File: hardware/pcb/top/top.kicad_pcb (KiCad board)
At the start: 2 copper layers, 65 x 120 mm, 33 parts, among them J1 OLED_128x32, J2 Conn_01x15, SW1 SLW-864574-5A-RA-N-D, SW2 RotaryEncoder_Switch

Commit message: finalized plate design
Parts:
- moved J1 1.77 mm to (121.2, 45.0)
- moved SW1 1.28 mm to (122.9, 36.7)
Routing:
- net OLED_SDA: track 119.9 -> 123.6 mm
- net +3.3V: track 136.4 -> 138.9 mm
- net OLED_SCL: track 119.7 -> 121.7 mm
- net BT_SELECT: track 198.0 -> 198.5 mm

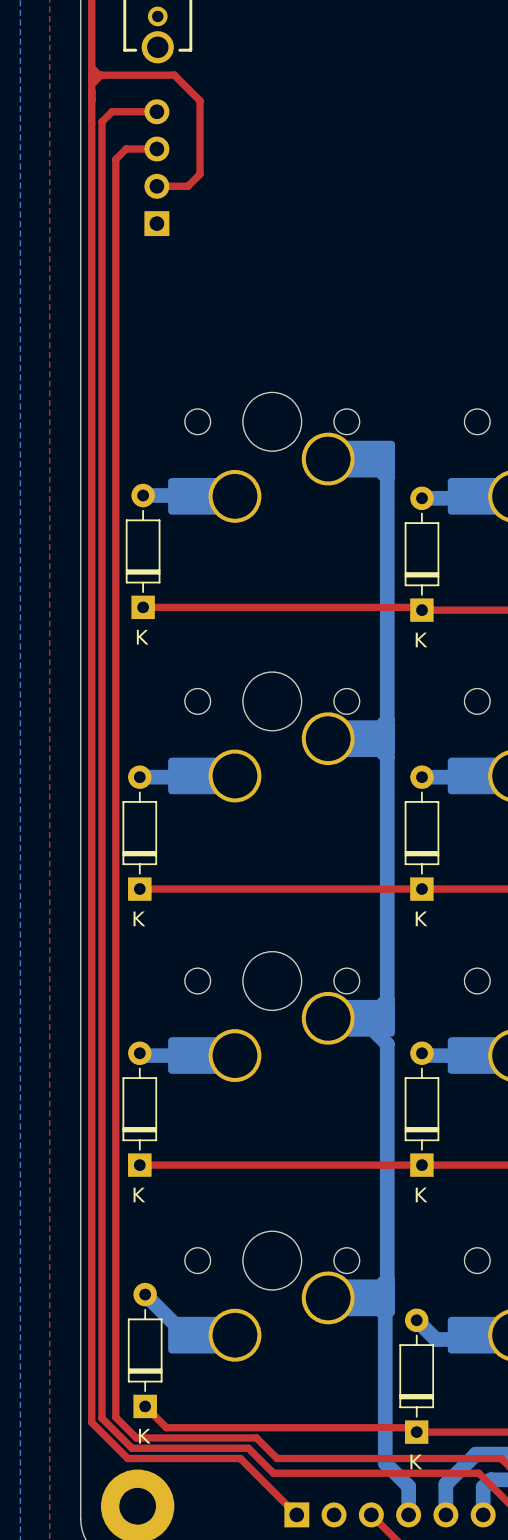
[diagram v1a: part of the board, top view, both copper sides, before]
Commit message: migrate kicad projects from v8 to v9
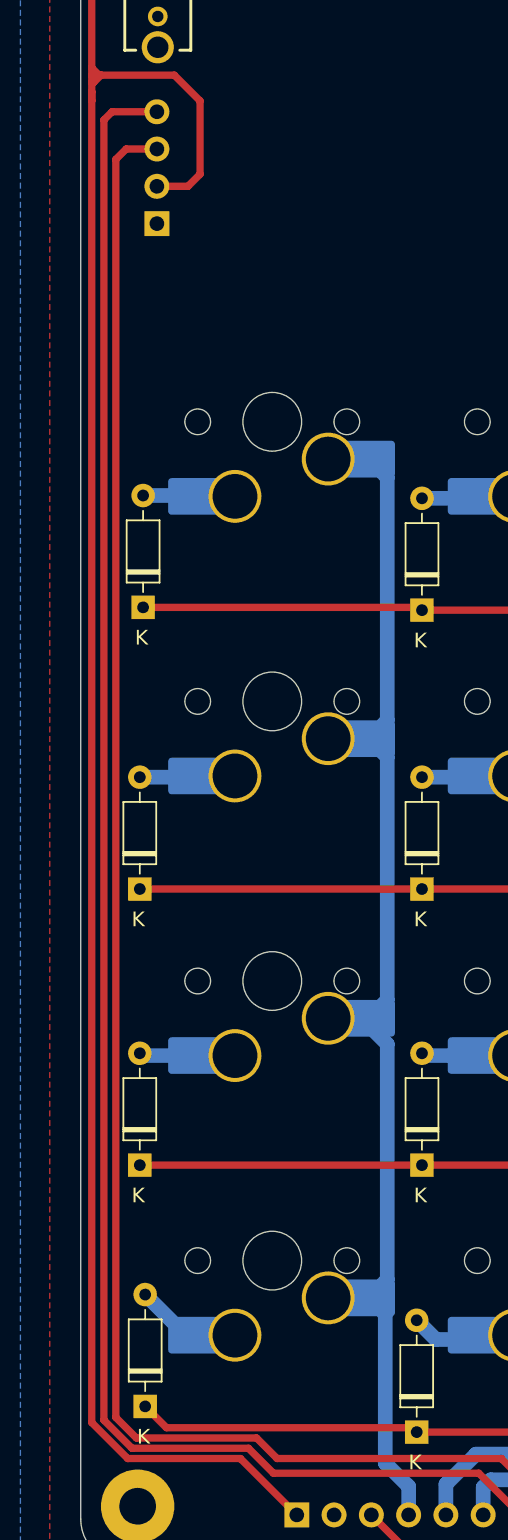
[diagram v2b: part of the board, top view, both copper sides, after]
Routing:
- net Net-(D10-A): track 4.49 -> 3.91 mm

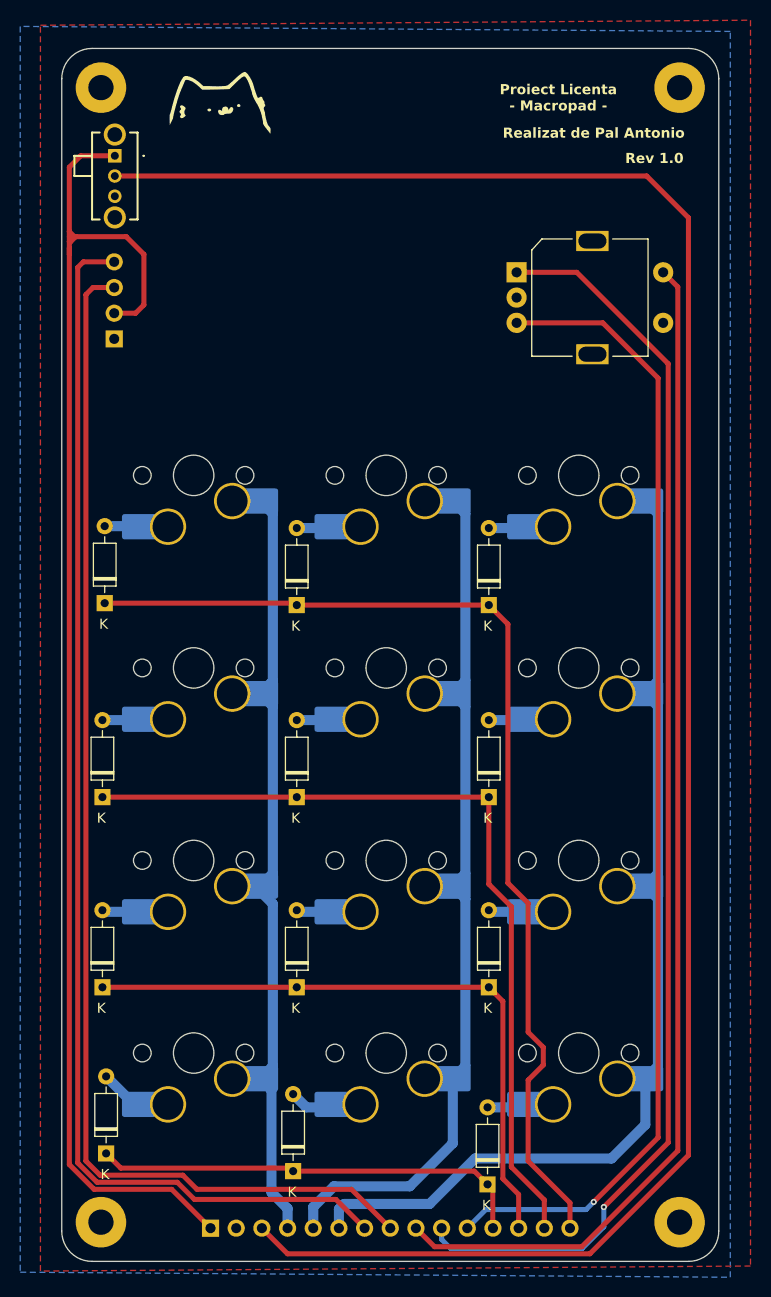
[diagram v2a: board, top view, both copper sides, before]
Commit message: Optimize routing and improve grounding
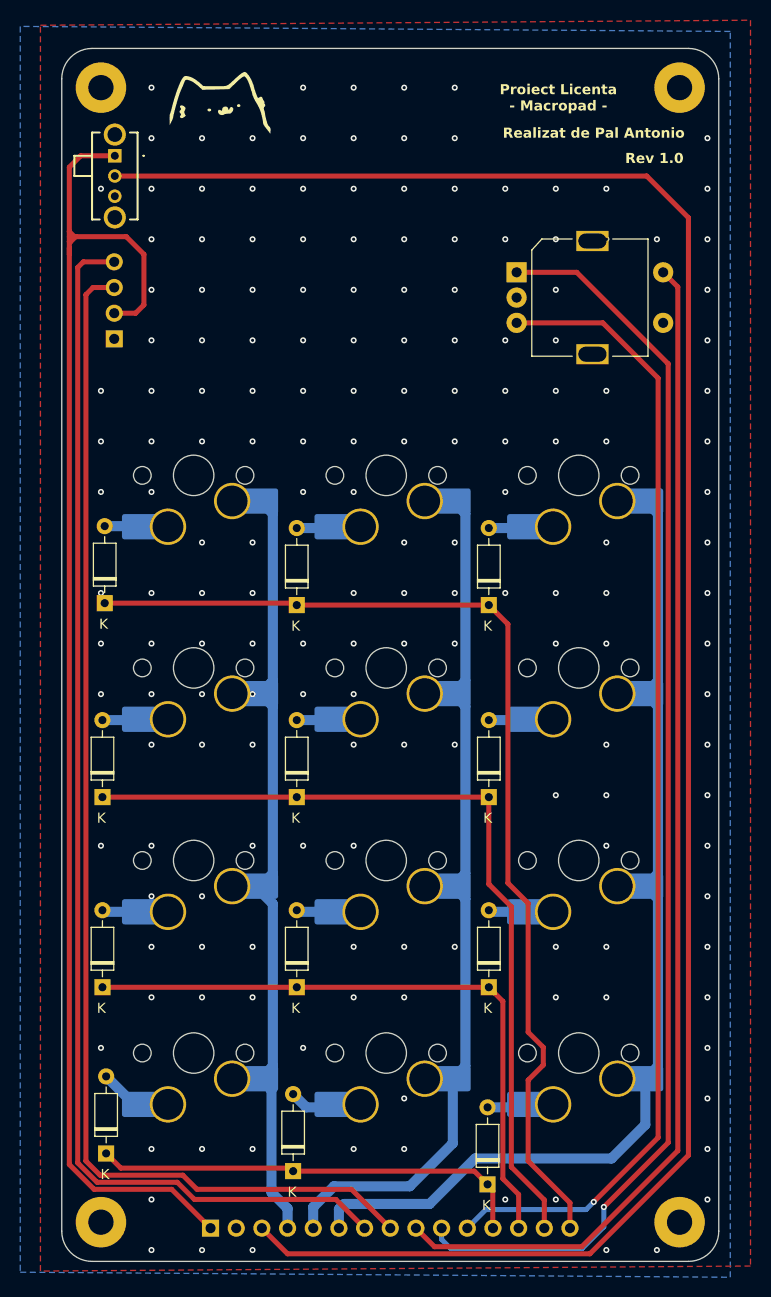
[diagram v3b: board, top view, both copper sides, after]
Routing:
- net GND: vias 0 -> 179

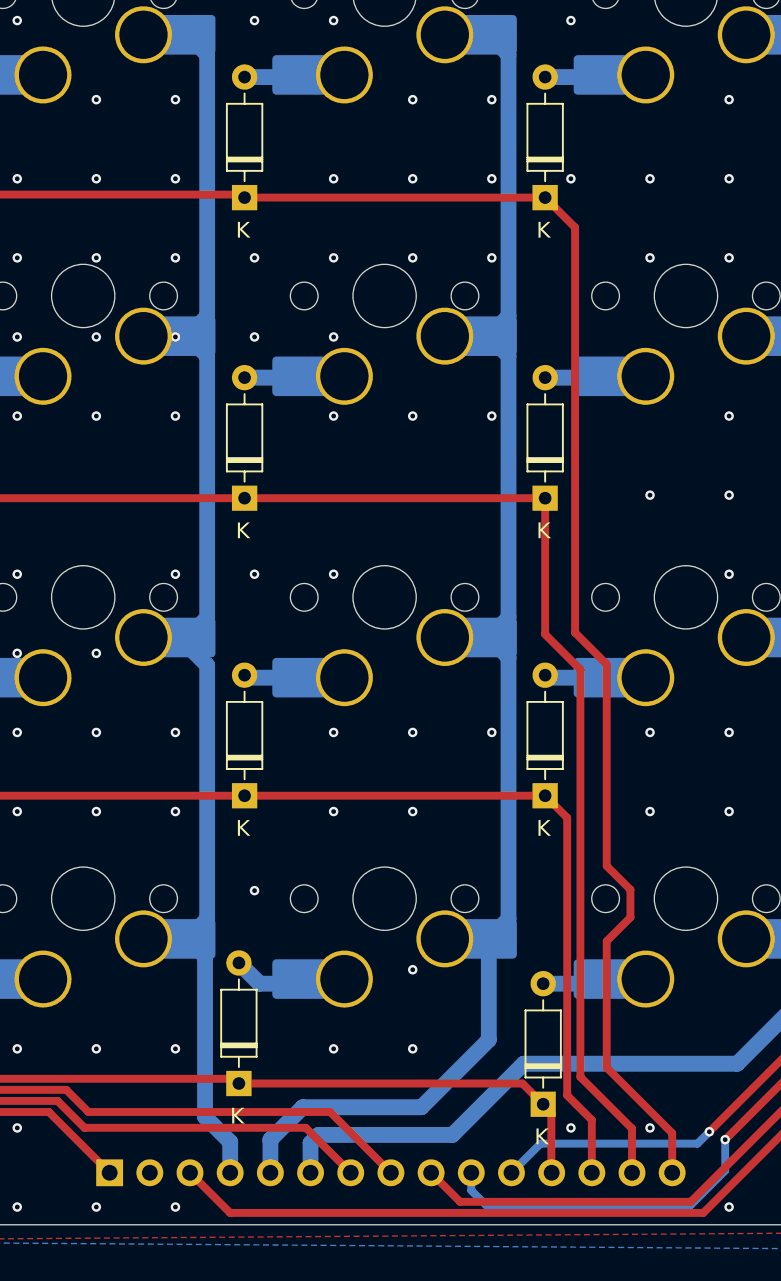
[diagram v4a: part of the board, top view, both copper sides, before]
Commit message: update documentation images, remove copper pours and vias from top plate, minor fixes
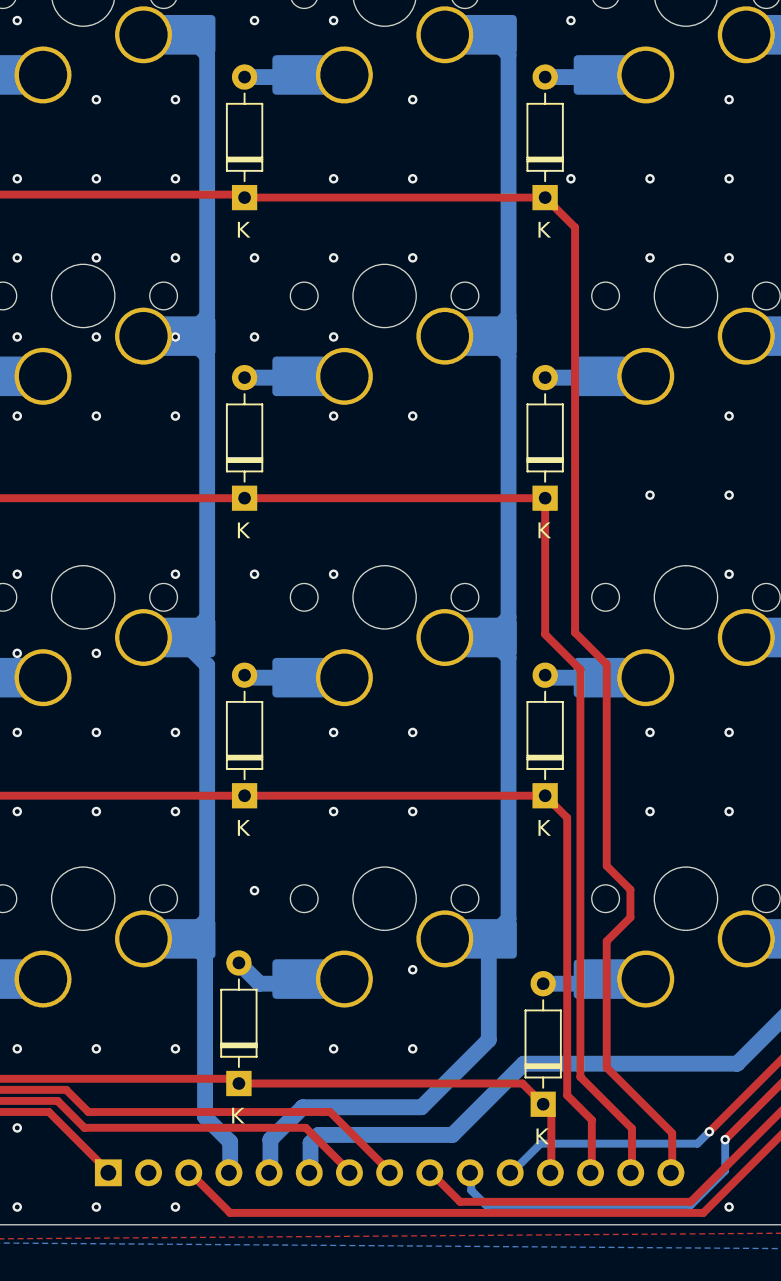
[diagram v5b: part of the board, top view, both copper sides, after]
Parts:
- moved J2 0.08 mm to (132.3, 142.8)
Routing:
- net GND: vias 179 -> 172

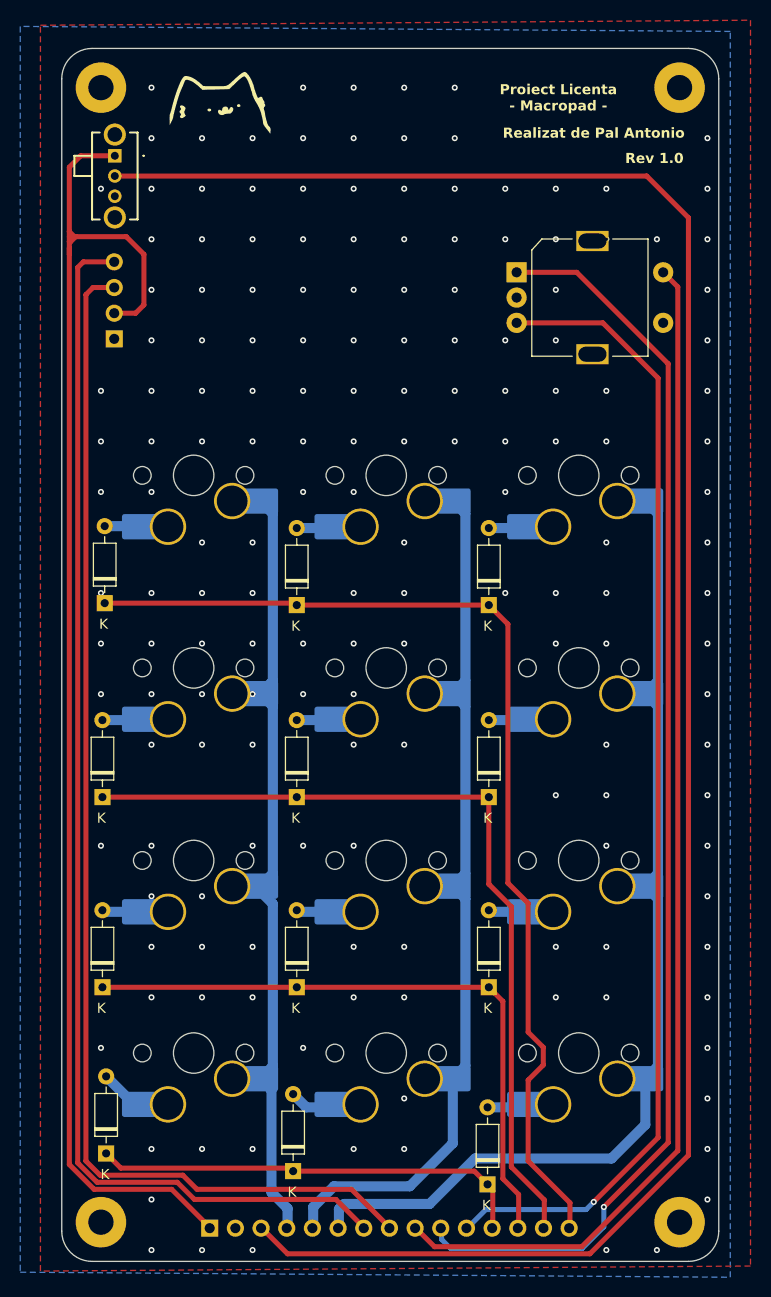
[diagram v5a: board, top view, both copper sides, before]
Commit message: changed m2.5 mh to m2, added screws and nuts to enclosure.FCStd
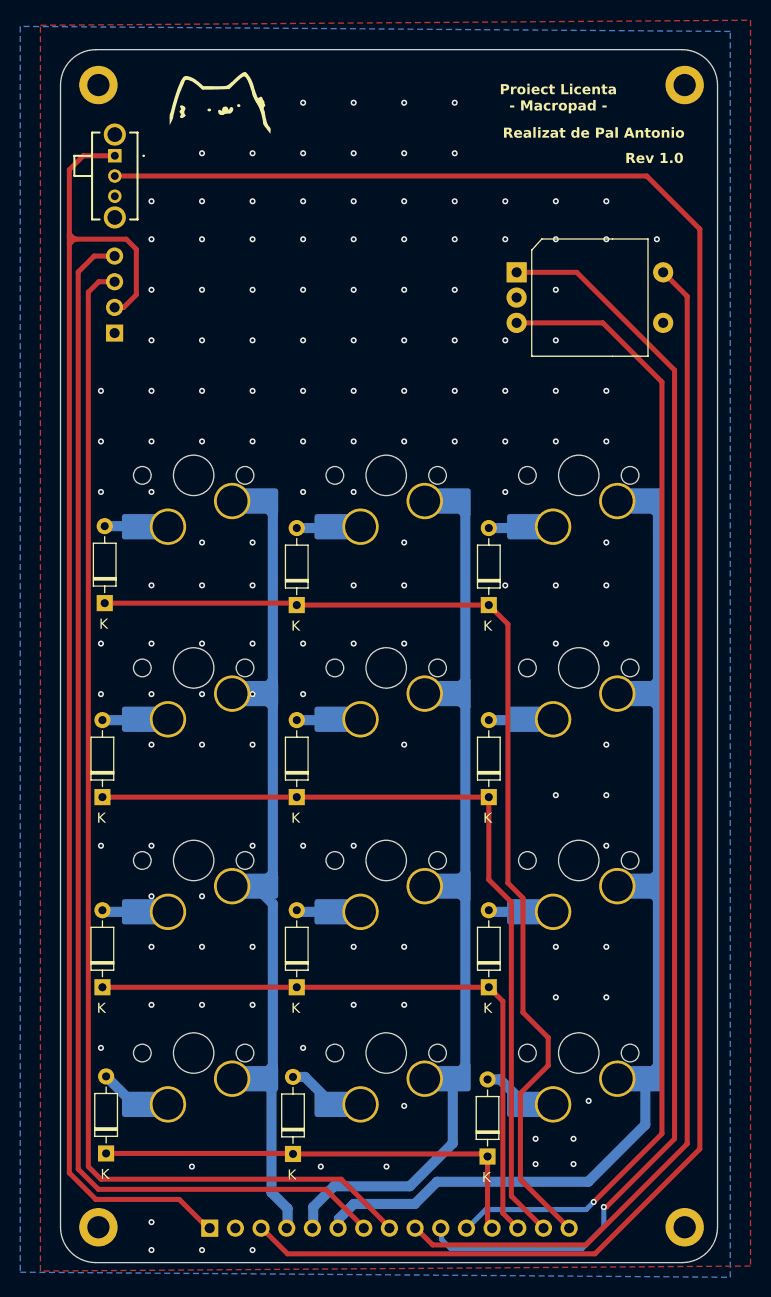
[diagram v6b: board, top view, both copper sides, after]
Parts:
- H1, H2, H3, H4: footprint MountingHole:MountingHole_2.5mm_Pad -> MountingHole:MountingHole_2.2mm_M2_DIN965_Pad
- moved D12 2.76 mm to (159.8, 135.7)
- moved D11 1.70 mm to (140.5, 135.4)
- moved H4 0.71 mm to (179.3, 142.7)
- moved J1 0.57 mm to (121.3, 44.4)
- moved H1 0.57 mm to (179.3, 29.7)
- moved H3 0.56 mm to (121.3, 142.7)
- moved H2 0.36 mm to (121.3, 29.7)
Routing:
- net ROW3: track 42.4 -> 45.8 mm
- net +3.3V: track 138.9 -> 136.4 mm
- net Net-(D12-A): track 3.41 -> 4.90 mm
- net BT_SELECT: track 198.5 -> 199.7 mm
- net ROW0: track 103.9 -> 105.0 mm
- net Net-(D11-A): track 4.14 -> 5.20 mm
- net ENC_SW: track 118.1 -> 118.9 mm
- net ENC_CLK: track 125.2 -> 125.9 mm
- net COL2: track 100.5 -> 99.9 mm
- net GND: track 0.00 -> 0.01 mm, vias 172 -> 145
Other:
- outline, holes or cut-outs redrawn

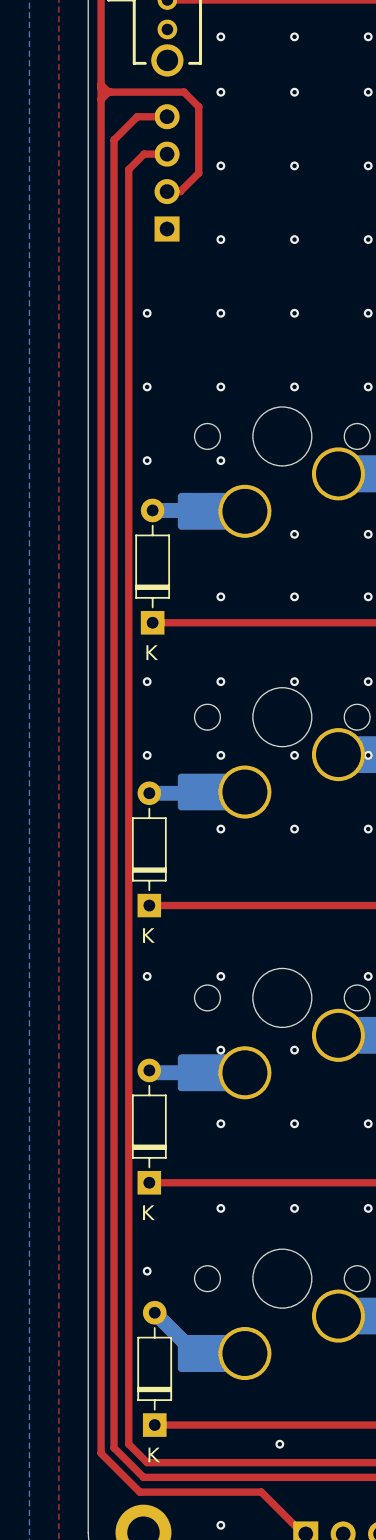
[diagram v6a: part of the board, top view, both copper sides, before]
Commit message: fixed positioning issues, changed the type of nuts holding the pcb
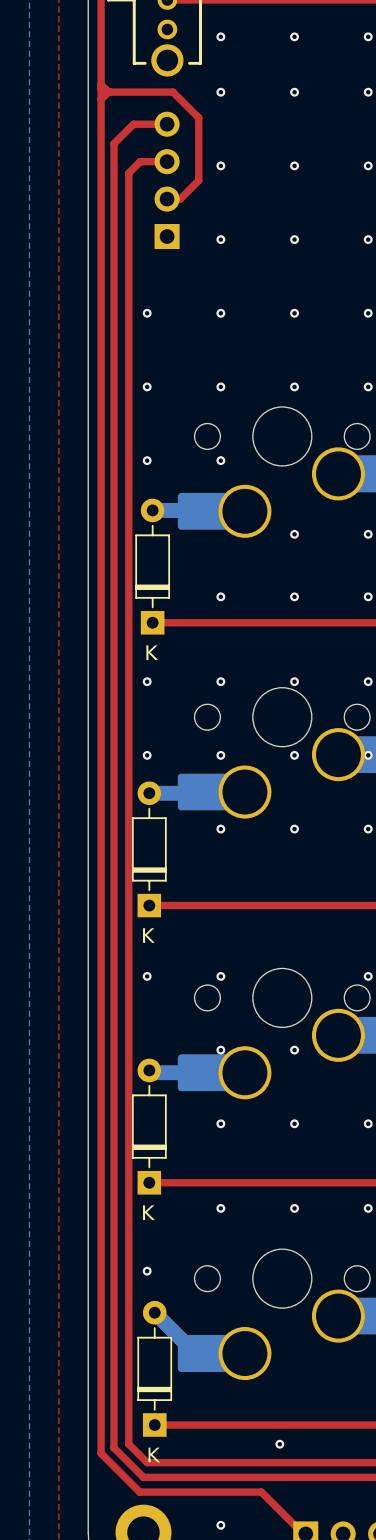
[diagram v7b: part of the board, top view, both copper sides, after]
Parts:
- moved J1 0.51 mm to (121.3, 44.9)
